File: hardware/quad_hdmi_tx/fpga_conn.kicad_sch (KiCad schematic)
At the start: 7 parts, among them J7 FPGA_J7, J8 FPGA_J8

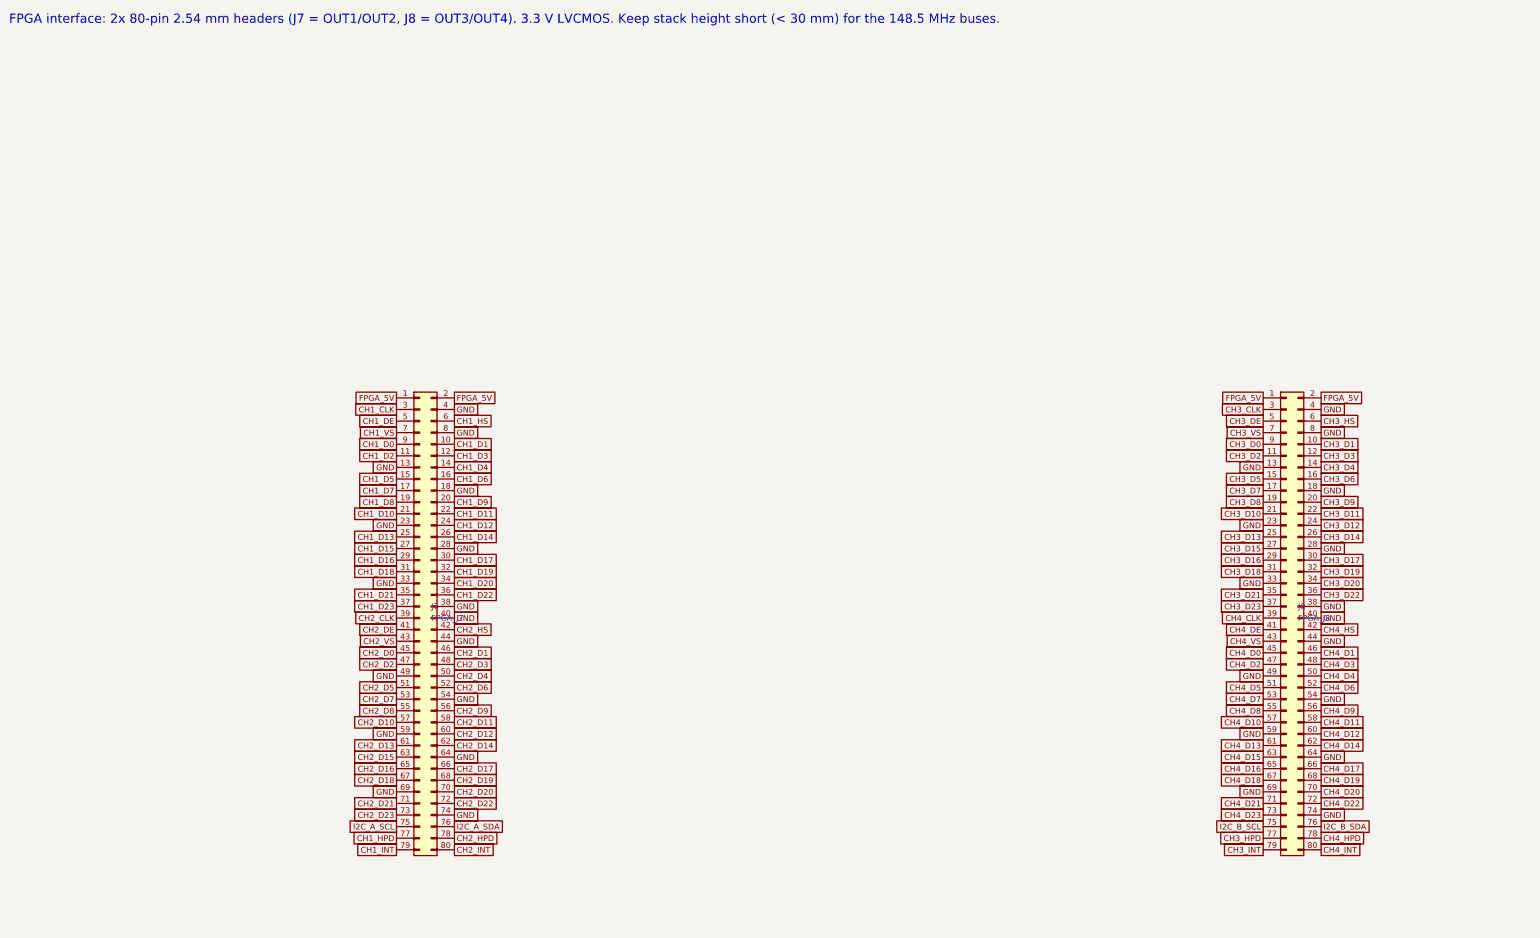
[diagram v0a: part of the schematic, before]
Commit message: 基板レイアウトの生成パイプラインを追加: 配置・外形・プレーン生成、自動配線、DRC、製造データ出力
- gen_pcb.py: ネットリストから 4 層基板 (115x110 mm) を生成。HDMI 上辺、TPD/ADV の向きを TMDS が交差しないよう配置
- route_pcb.py: DSN 書き出し / SES 取り込み、外層 GND ベタ、ゾーン塗り、DRC
- layout_report.py: 配線長、ビア数、TMDS ペア長差、DRC 集計
- export_fab.sh: ガーバー、ドリル、CPL、各層 PDF
- J7 = OUT1/OUT3、J8 = OUT2/OUT4 にヘッダ割り当てを変更 (回路図・ネットリスト再生成)
- README にレイアウト節 (配置図、層構成、ルール、パイプライン)

Co-Authored-By: Claude Fable 5.1 <noreply@anthropic.com>
Claude-Session: https://claude.ai/code/session_01JGo25NCpKCcdkj7JC5mDdQ
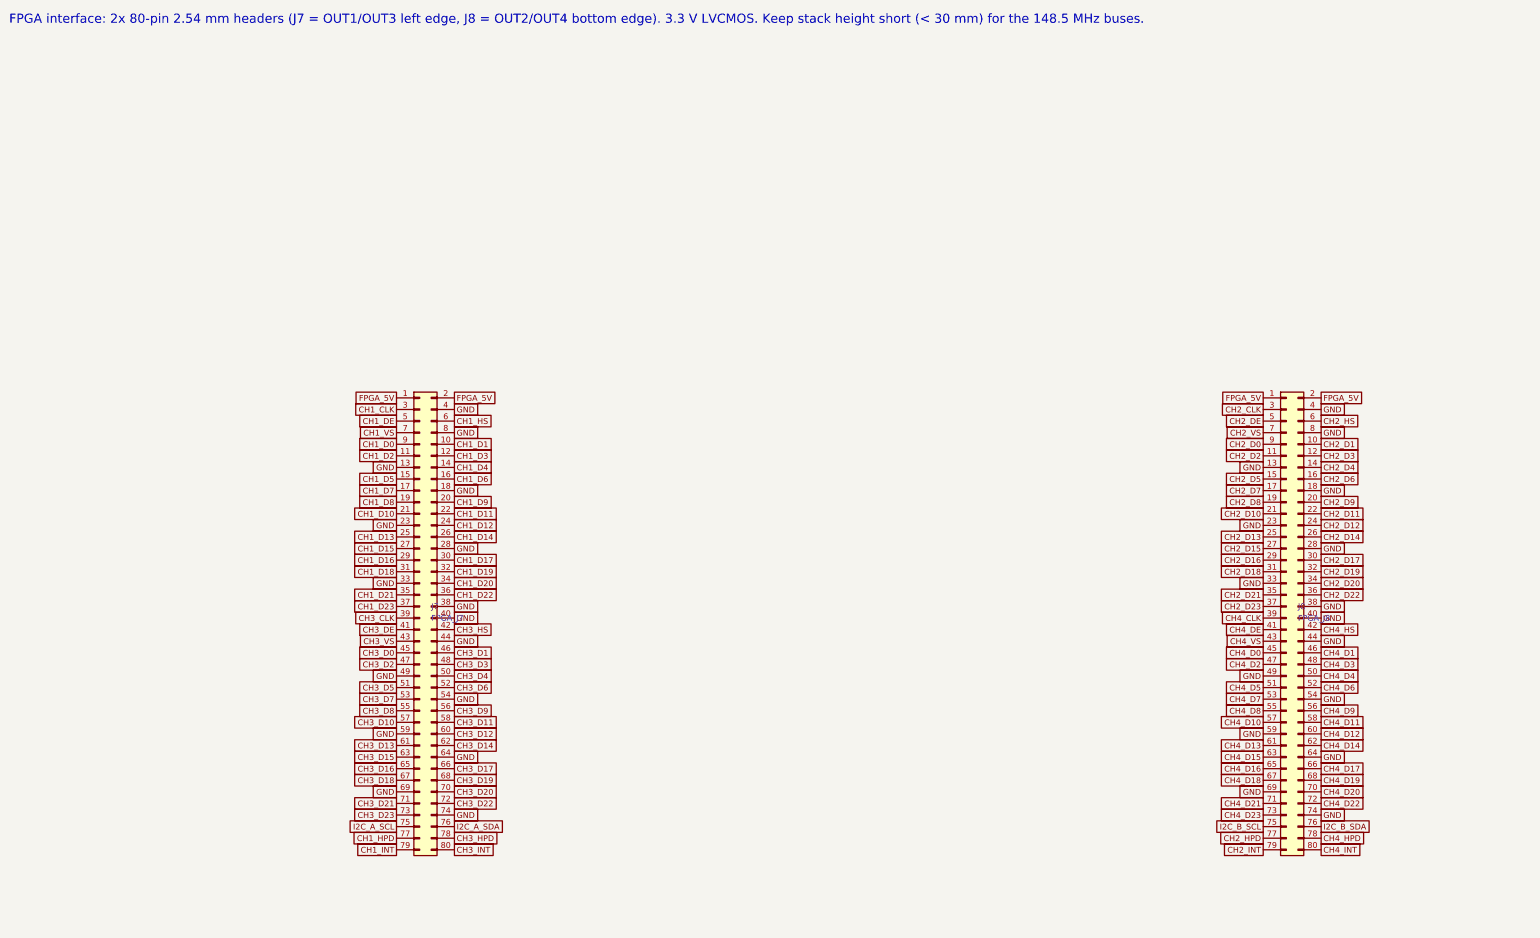
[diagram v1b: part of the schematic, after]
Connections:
- net CH2_CLK: now also J8.3 (Pin_3); no longer J7.39 (Pin_39)
- net CH2_D0: now also J8.9 (Pin_9); no longer J7.45 (Pin_45)
- net CH2_D1: now also J8.10 (Pin_10); no longer J7.46 (Pin_46)
- net CH2_D10: now also J8.21 (Pin_21); no longer J7.57 (Pin_57)
- net CH2_D11: now also J8.22 (Pin_22); no longer J7.58 (Pin_58)
- net CH2_D12: now also J8.24 (Pin_24); no longer J7.60 (Pin_60)
- net CH2_D13: now also J8.25 (Pin_25); no longer J7.61 (Pin_61)
- net CH2_D14: now also J8.26 (Pin_26); no longer J7.62 (Pin_62)
- net CH2_D15: now also J8.27 (Pin_27); no longer J7.63 (Pin_63)
- net CH2_D16: now also J8.29 (Pin_29); no longer J7.65 (Pin_65)
- net CH2_D17: now also J8.30 (Pin_30); no longer J7.66 (Pin_66)
- net CH2_D18: now also J8.31 (Pin_31); no longer J7.67 (Pin_67)
- net CH2_D19: now also J8.32 (Pin_32); no longer J7.68 (Pin_68)
- net CH2_D2: now also J8.11 (Pin_11); no longer J7.47 (Pin_47)
- net CH2_D20: now also J8.34 (Pin_34); no longer J7.70 (Pin_70)
- net CH2_D21: now also J8.35 (Pin_35); no longer J7.71 (Pin_71)
- net CH2_D22: now also J8.36 (Pin_36); no longer J7.72 (Pin_72)
- net CH2_D23: now also J8.37 (Pin_37); no longer J7.73 (Pin_73)
- net CH2_D3: now also J8.12 (Pin_12); no longer J7.48 (Pin_48)
- net CH2_D4: now also J8.14 (Pin_14); no longer J7.50 (Pin_50)
- net CH2_D5: now also J8.15 (Pin_15); no longer J7.51 (Pin_51)
- net CH2_D6: now also J8.16 (Pin_16); no longer J7.52 (Pin_52)
- net CH2_D7: now also J8.17 (Pin_17); no longer J7.53 (Pin_53)
- net CH2_D8: now also J8.19 (Pin_19); no longer J7.55 (Pin_55)
- net CH2_D9: now also J8.20 (Pin_20); no longer J7.56 (Pin_56)
- net CH2_DE: now also J8.5 (Pin_5); no longer J7.41 (Pin_41)
- net CH2_HPD: now also J8.77 (Pin_77); no longer J7.78 (Pin_78)
- net CH2_HS: now also J8.6 (Pin_6); no longer J7.42 (Pin_42)
- net CH2_INT: now also J8.79 (Pin_79); no longer J7.80 (Pin_80)
- net CH2_VS: now also J8.7 (Pin_7); no longer J7.43 (Pin_43)
- net CH3_CLK: now also J7.39 (Pin_39); no longer J8.3 (Pin_3)
- net CH3_D0: now also J7.45 (Pin_45); no longer J8.9 (Pin_9)
- net CH3_D1: now also J7.46 (Pin_46); no longer J8.10 (Pin_10)
- net CH3_D10: now also J7.57 (Pin_57); no longer J8.21 (Pin_21)
- net CH3_D11: now also J7.58 (Pin_58); no longer J8.22 (Pin_22)
- net CH3_D12: now also J7.60 (Pin_60); no longer J8.24 (Pin_24)
- net CH3_D13: now also J7.61 (Pin_61); no longer J8.25 (Pin_25)
- net CH3_D14: now also J7.62 (Pin_62); no longer J8.26 (Pin_26)
- net CH3_D15: now also J7.63 (Pin_63); no longer J8.27 (Pin_27)
- net CH3_D16: now also J7.65 (Pin_65); no longer J8.29 (Pin_29)
- net CH3_D17: now also J7.66 (Pin_66); no longer J8.30 (Pin_30)
- net CH3_D18: now also J7.67 (Pin_67); no longer J8.31 (Pin_31)
- net CH3_D19: now also J7.68 (Pin_68); no longer J8.32 (Pin_32)
- net CH3_D2: now also J7.47 (Pin_47); no longer J8.11 (Pin_11)
- net CH3_D20: now also J7.70 (Pin_70); no longer J8.34 (Pin_34)
- net CH3_D21: now also J7.71 (Pin_71); no longer J8.35 (Pin_35)
- net CH3_D22: now also J7.72 (Pin_72); no longer J8.36 (Pin_36)
- net CH3_D23: now also J7.73 (Pin_73); no longer J8.37 (Pin_37)
- net CH3_D3: now also J7.48 (Pin_48); no longer J8.12 (Pin_12)
- net CH3_D4: now also J7.50 (Pin_50); no longer J8.14 (Pin_14)
- net CH3_D5: now also J7.51 (Pin_51); no longer J8.15 (Pin_15)
- net CH3_D6: now also J7.52 (Pin_52); no longer J8.16 (Pin_16)
- net CH3_D7: now also J7.53 (Pin_53); no longer J8.17 (Pin_17)
- net CH3_D8: now also J7.55 (Pin_55); no longer J8.19 (Pin_19)
- net CH3_D9: now also J7.56 (Pin_56); no longer J8.20 (Pin_20)
- net CH3_DE: now also J7.41 (Pin_41); no longer J8.5 (Pin_5)
- net CH3_HPD: now also J7.78 (Pin_78); no longer J8.77 (Pin_77)
- net CH3_HS: now also J7.42 (Pin_42); no longer J8.6 (Pin_6)
- net CH3_INT: now also J7.80 (Pin_80); no longer J8.79 (Pin_79)
- net CH3_VS: now also J7.43 (Pin_43); no longer J8.7 (Pin_7)
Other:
- note added: "FPGA interface: 2x 80-pin 2.54 mm headers (J7 = OUT1/OUT3 left edge, J8 = OUT2/OUT4 bottom edge). 3.3 V LVCMOS. Keep stack height short (< 30 mm) for the 148.5 MHz buses."
- note removed: "FPGA interface: 2x 80-pin 2.54 mm headers (J7 = OUT1/OUT2, J8 = OUT3/OUT4). 3.3 V LVCMOS. Keep stack height short (< 30 mm) for the 148.5 MHz buses."

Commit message: レイアウト rev B: 115 × 38 mm の細長い 6 層基板に再配置、ヘッダ配線を全数固定して DRC 未接続 0 / クリアランス違反 0
- 基板を HDMI 4 個分の横幅 (115 mm) × 縦 38 mm (横の 1/3) に変更、6 層 (F / GND / SIG1 / SIG2 / PWR / B)
- FPGA ヘッダ 2×40 を裏面に 2 本、長辺と平行に配置。ヘッダの列が各 ADV7513 の真下に来る
- J7/J8 のピン割り当てを配線経路に合わせて変更 (J7 = ADV 左辺の D13-23 + D1/D2/D4/D5/D10、J8 = 下辺の残り + CLK/DE/HS/VS/HPD/INT)
- RGB バス 30 本 × 4 ch、DDC/CEC/HPD、AVDD/PVDD の一部、FPGA_5V を gen_pcb.py で内層に固定配線 (交差しないレーン割り当て)
- 部品の再配置 (C01/C16/C20/R2/R4、左の 1V8 コンデンサ列を x=cx-10.3 へ)、1V8 の島の首を広げてプレーンの連続を確保
- FreeRouting 1.9 (-mp 24 -oit 1.0、約 10 分) で残りを配線: 配線 2010 本、ビア 634 個、TMDS はビアなし・ペア内長差 0.47 mm 以下
- ガーバー / ドリル / CPL / 各層 PDF と docs の画像を再生成、README と fpga_header_pinmap.csv を更新

Co-Authored-By: Claude Fable 5.1 <noreply@anthropic.com>
Claude-Session: https://claude.ai/code/session_01JGo25NCpKCcdkj7JC5mDdQ
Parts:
- J7, J8: footprint Connector_PinHeader_2.54mm:PinHeader_2x40_P2.54mm_Vertical -> Connector_PinHeader_2.54mm:PinHeader_2x40_P2.54mm_Vertical_SMD; MPN PH2-80-UA -> TSM-140-01-L-DV
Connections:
- net CH1_CLK: now also J8.3 (Pin_3); no longer J7.3 (Pin_3)
- net CH1_D0: now also J8.18 (Pin_18); no longer J7.9 (Pin_9)
- net CH1_D1: now also J7.18 (Pin_18); no longer J7.10 (Pin_10)
- net CH1_D10: now also J7.16 (Pin_16); no longer J7.21 (Pin_21)
- net CH1_D11: now also J8.8 (Pin_8); no longer J7.22 (Pin_22)
- net CH1_D12: now also J8.6 (Pin_6); no longer J7.24 (Pin_24)
- net CH1_D13: now also J7.5 (Pin_5); no longer J7.25 (Pin_25)
- net CH1_D14: now also J7.7 (Pin_7); no longer J7.26 (Pin_26)
- net CH1_D15: now also J7.6 (Pin_6); no longer J7.27 (Pin_27)
- net CH1_D16: now also J7.11 (Pin_11); no longer J7.29 (Pin_29)
- net CH1_D17: now also J7.4 (Pin_4); no longer J7.30 (Pin_30)
- net CH1_D18: now also J7.1 (Pin_1); no longer J7.31 (Pin_31)
- net CH1_D19: now also J7.2 (Pin_2); no longer J7.32 (Pin_32)
- net CH1_D2: now also J7.17 (Pin_17); no longer J7.11 (Pin_11)
- net CH1_D20: now also J7.13 (Pin_13); no longer J7.34 (Pin_34)
- net CH1_D21: now also J7.15 (Pin_15); no longer J7.35 (Pin_35)
- net CH1_D22: now also J7.9 (Pin_9); no longer J7.36 (Pin_36)
- net CH1_D23: now also J7.3 (Pin_3); no longer J7.37 (Pin_37)
- net CH1_D3: now also J8.12 (Pin_12); no longer J7.12 (Pin_12)
- net CH1_D4: now also J7.20 (Pin_20); no longer J7.14 (Pin_14)
- net CH1_D5: now also J7.19 (Pin_19); no longer J7.15 (Pin_15)
- net CH1_D6: now also J8.1 (Pin_1); no longer J7.16 (Pin_16)
- net CH1_D7: now also J8.2 (Pin_2); no longer J7.17 (Pin_17)
- net CH1_D8: now also J8.10 (Pin_10); no longer J7.19 (Pin_19)
- net CH1_D9: now also J8.4 (Pin_4); no longer J7.20 (Pin_20)
- net CH1_DE: now also J8.17 (Pin_17); no longer J7.5 (Pin_5)
- net CH1_HPD: now also J8.15 (Pin_15); no longer J7.77 (Pin_77)
- net CH1_HS: now also J8.14 (Pin_14); no longer J7.6 (Pin_6)
- net CH1_INT: now also J8.5 (Pin_5); no longer J7.79 (Pin_79)
- net CH1_VS: now also J8.16 (Pin_16); no longer J7.7 (Pin_7)
- net CH2_CLK: now also J8.23 (Pin_23); no longer J8.3 (Pin_3)
- net CH2_D0: now also J8.38 (Pin_38); no longer J8.9 (Pin_9)
- net CH2_D1: now also J7.38 (Pin_38); no longer J8.10 (Pin_10)
- net CH2_D10: now also J7.36 (Pin_36); no longer J8.21 (Pin_21)
- net CH2_D11: now also J8.28 (Pin_28); no longer J8.22 (Pin_22)
- net CH2_D12: now also J8.26 (Pin_26); no longer J8.24 (Pin_24)
- net CH2_D13: now also J7.25 (Pin_25); no longer J8.25 (Pin_25)
- net CH2_D14: now also J7.27 (Pin_27); no longer J8.26 (Pin_26)
- net CH2_D15: now also J7.26 (Pin_26); no longer J8.27 (Pin_27)
- net CH2_D16: now also J7.31 (Pin_31); no longer J8.29 (Pin_29)
- net CH2_D17: now also J7.24 (Pin_24); no longer J8.30 (Pin_30)
- net CH2_D18: now also J7.21 (Pin_21); no longer J8.31 (Pin_31)
- net CH2_D19: now also J7.22 (Pin_22); no longer J8.32 (Pin_32)
- net CH2_D2: now also J7.37 (Pin_37); no longer J8.11 (Pin_11)
- net CH2_D20: now also J7.33 (Pin_33); no longer J8.34 (Pin_34)
- net CH2_D21: now also J7.35 (Pin_35); no longer J8.35 (Pin_35)
- net CH2_D22: now also J7.29 (Pin_29); no longer J8.36 (Pin_36)
- net CH2_D23: now also J7.23 (Pin_23); no longer J8.37 (Pin_37)
- net CH2_D3: now also J8.32 (Pin_32); no longer J8.12 (Pin_12)
- net CH2_D4: now also J7.40 (Pin_40); no longer J8.14 (Pin_14)
- net CH2_D5: now also J7.39 (Pin_39); no longer J8.15 (Pin_15)
- net CH2_D6: now also J8.21 (Pin_21); no longer J8.16 (Pin_16)
- net CH2_D7: now also J8.22 (Pin_22); no longer J8.17 (Pin_17)
- net CH2_D8: now also J8.30 (Pin_30); no longer J8.19 (Pin_19)
- net CH2_D9: now also J8.24 (Pin_24); no longer J8.20 (Pin_20)
- net CH2_DE: now also J8.37 (Pin_37); no longer J8.5 (Pin_5)
- net CH2_HPD: now also J8.35 (Pin_35); no longer J8.77 (Pin_77)
- net CH2_HS: now also J8.34 (Pin_34); no longer J8.6 (Pin_6)
- net CH2_INT: now also J8.25 (Pin_25); no longer J8.79 (Pin_79)
- net CH2_VS: now also J8.36 (Pin_36); no longer J8.7 (Pin_7)
- net CH3_CLK: now also J8.43 (Pin_43); no longer J7.39 (Pin_39)
- net CH3_D0: now also J8.58 (Pin_58); no longer J7.45 (Pin_45)
- net CH3_D1: now also J7.58 (Pin_58); no longer J7.46 (Pin_46)
- net CH3_D10: now also J7.56 (Pin_56); no longer J7.57 (Pin_57)
- net CH3_D11: now also J8.48 (Pin_48); no longer J7.58 (Pin_58)
- net CH3_D12: now also J8.46 (Pin_46); no longer J7.60 (Pin_60)
- net CH3_D13: now also J7.45 (Pin_45); no longer J7.61 (Pin_61)
- net CH3_D14: now also J7.47 (Pin_47); no longer J7.62 (Pin_62)
- net CH3_D15: now also J7.46 (Pin_46); no longer J7.63 (Pin_63)
- net CH3_D16: now also J7.51 (Pin_51); no longer J7.65 (Pin_65)
- net CH3_D17: now also J7.44 (Pin_44); no longer J7.66 (Pin_66)
- net CH3_D18: now also J7.41 (Pin_41); no longer J7.67 (Pin_67)
- net CH3_D19: now also J7.42 (Pin_42); no longer J7.68 (Pin_68)
- net CH3_D2: now also J7.57 (Pin_57); no longer J7.47 (Pin_47)
- net CH3_D20: now also J7.53 (Pin_53); no longer J7.70 (Pin_70)
- net CH3_D21: now also J7.55 (Pin_55); no longer J7.71 (Pin_71)
- net CH3_D22: now also J7.49 (Pin_49); no longer J7.72 (Pin_72)
- net CH3_D23: now also J7.43 (Pin_43); no longer J7.73 (Pin_73)
- net CH3_D3: now also J8.52 (Pin_52); no longer J7.48 (Pin_48)
- net CH3_D4: now also J7.60 (Pin_60); no longer J7.50 (Pin_50)
- net CH3_D5: now also J7.59 (Pin_59); no longer J7.51 (Pin_51)
- net CH3_D6: now also J8.41 (Pin_41); no longer J7.52 (Pin_52)
- net CH3_D7: now also J8.42 (Pin_42); no longer J7.53 (Pin_53)
- net CH3_D8: now also J8.50 (Pin_50); no longer J7.55 (Pin_55)
- net CH3_D9: now also J8.44 (Pin_44); no longer J7.56 (Pin_56)
- net CH3_DE: now also J8.57 (Pin_57); no longer J7.41 (Pin_41)
- net CH3_HPD: now also J8.55 (Pin_55); no longer J7.78 (Pin_78)
- net CH3_HS: now also J8.54 (Pin_54); no longer J7.42 (Pin_42)
- net CH3_INT: now also J8.45 (Pin_45); no longer J7.80 (Pin_80)
- net CH3_VS: now also J8.56 (Pin_56); no longer J7.43 (Pin_43)
- net CH4_CLK: now also J8.63 (Pin_63); no longer J8.39 (Pin_39)
- net CH4_D0: now also J8.78 (Pin_78); no longer J8.45 (Pin_45)
- net CH4_D1: now also J7.78 (Pin_78); no longer J8.46 (Pin_46)
- net CH4_D10: now also J7.76 (Pin_76); no longer J8.57 (Pin_57)
- net CH4_D11: now also J8.68 (Pin_68); no longer J8.58 (Pin_58)
- net CH4_D12: now also J8.66 (Pin_66); no longer J8.60 (Pin_60)
- net CH4_D13: now also J7.65 (Pin_65); no longer J8.61 (Pin_61)
- net CH4_D14: now also J7.67 (Pin_67); no longer J8.62 (Pin_62)
- net CH4_D15: now also J7.66 (Pin_66); no longer J8.63 (Pin_63)
- net CH4_D16: now also J7.71 (Pin_71); no longer J8.65 (Pin_65)
- net CH4_D17: now also J7.64 (Pin_64); no longer J8.66 (Pin_66)
- net CH4_D18: now also J7.61 (Pin_61); no longer J8.67 (Pin_67)
- net CH4_D19: now also J7.62 (Pin_62); no longer J8.68 (Pin_68)
- net CH4_D2: now also J7.77 (Pin_77); no longer J8.47 (Pin_47)
- net CH4_D20: now also J7.73 (Pin_73); no longer J8.70 (Pin_70)
- net CH4_D21: now also J7.75 (Pin_75); no longer J8.71 (Pin_71)
- net CH4_D22: now also J7.69 (Pin_69); no longer J8.72 (Pin_72)
- net CH4_D23: now also J7.63 (Pin_63); no longer J8.73 (Pin_73)
- net CH4_D3: now also J8.72 (Pin_72); no longer J8.48 (Pin_48)
- net CH4_D4: now also J7.80 (Pin_80); no longer J8.50 (Pin_50)
- net CH4_D5: now also J7.79 (Pin_79); no longer J8.51 (Pin_51)
- net CH4_D6: now also J8.61 (Pin_61); no longer J8.52 (Pin_52)
- net CH4_D7: now also J8.62 (Pin_62); no longer J8.53 (Pin_53)
- net CH4_D8: now also J8.70 (Pin_70); no longer J8.55 (Pin_55)
- net CH4_D9: now also J8.64 (Pin_64); no longer J8.56 (Pin_56)
- net CH4_DE: now also J8.77 (Pin_77); no longer J8.41 (Pin_41)
- net CH4_HPD: now also J8.75 (Pin_75); no longer J8.78 (Pin_78)
- net CH4_HS: now also J8.74 (Pin_74); no longer J8.42 (Pin_42)
- net CH4_INT: now also J8.65 (Pin_65); no longer J8.80 (Pin_80)
- net CH4_VS: now also J8.76 (Pin_76); no longer J8.43 (Pin_43)
- net FPGA_5V: now also J8.39 (Pin_39), J8.40 (Pin_40); no longer J7.1 (Pin_1), J7.2 (Pin_2), J8.1 (Pin_1), J8.2 (Pin_2)
- net GND: now also J7.10 (Pin_10), J7.12 (Pin_12), J7.14 (Pin_14), J7.30 (Pin_30), J7.32 (Pin_32), J7.34 (Pin_34), J7.48 (Pin_48), J7.50 (Pin_50), J7.52 (Pin_52), J7.68 (Pin_68), J7.70 (Pin_70), J7.72 (Pin_72), J8.11 (Pin_11), J8.27 (Pin_27), J8.29 (Pin_29), J8.31 (Pin_31), J8.47 (Pin_47), J8.51 (Pin_51), J8.53 (Pin_53), J8.67 (Pin_67), J8.7 (Pin_7), J8.71 (Pin_71), J8.73 (Pin_73), J8.79 (Pin_79), J8.80 (Pin_80), J8.9 (Pin_9); no longer J7.13 (Pin_13), J7.18 (Pin_18), J7.23 (Pin_23), J7.33 (Pin_33), J7.38 (Pin_38), J7.4 (Pin_4), J7.40 (Pin_40), J7.44 (Pin_44), J7.49 (Pin_49), J7.59 (Pin_59), J7.64 (Pin_64), J7.69 (Pin_69), J8.18 (Pin_18), J8.23 (Pin_23), J8.28 (Pin_28), J8.38 (Pin_38), J8.4 (Pin_4), J8.40 (Pin_40), J8.44 (Pin_44), J8.54 (Pin_54), J8.59 (Pin_59), J8.64 (Pin_64), J8.74 (Pin_74), J8.8 (Pin_8)
- net I2C_A_SCL: now also J8.19 (Pin_19); no longer J7.75 (Pin_75)
- net I2C_A_SDA: now also J8.20 (Pin_20); no longer J7.76 (Pin_76)
- net I2C_B_SCL: now also J8.59 (Pin_59); no longer J8.75 (Pin_75)
- net I2C_B_SDA: now also J8.60 (Pin_60); no longer J8.76 (Pin_76)
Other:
- note added: "FPGA interface: 2x 80-pin 2.54 mm SMD headers on the bottom side, parallel to the long edge. Header column k (pins 2k-1/2k) sits under the ADV7513 of OUT ceil(k/10): J7 = D13-D23 (+D1/D2/D4/D5/D10), J8 = D0-D9/D11/D12/CLK/DE/HS/VS/HPD/INT (+I2C, 5V). 3.3 V LVCMOS, 148.5 MHz SDR: keep ribbon cables short (< 15 cm)."
- note added: "JP1 closed: this board powers the FPGA board through J8 pins 39-40 (FPGA_5V). Leave open if the FPGA board has its own supply."
- note removed: "FPGA interface: 2x 80-pin 2.54 mm headers (J7 = OUT1/OUT3 left edge, J8 = OUT2/OUT4 bottom edge). 3.3 V LVCMOS. Keep stack height short (< 30 mm) for the 148.5 MHz buses."
- note removed: "JP1 closed: this board powers the FPGA board through J7/J8 pins 1-2. Leave open if the FPGA board has its own supply."
